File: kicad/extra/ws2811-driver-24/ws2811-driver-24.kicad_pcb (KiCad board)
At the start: 2 copper layers, 140 x 25 mm, 23 parts, among them J1 Conn_01x13_Pin, J2 Conn_01x13_Pin, J3 RJ45 IN, J4 RJ45 OUT, J5 Conn_01x03_Pin, U1 WS2811, U2 WS2811, U3 WS2811, U4 WS2811, U5 WS2811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

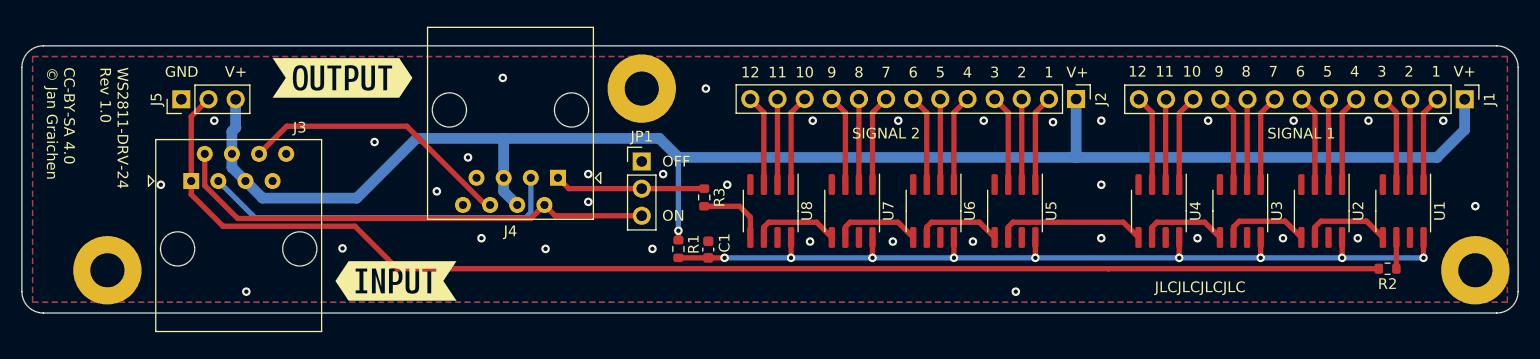
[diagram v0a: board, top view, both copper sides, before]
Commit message: feat: Rework WS2811 boards (Rev 2.0)
* Change RJ45 pinout: The data signal is always paired with a ground
  line to increase signal stability, and the changed wireing eases the
  traces on the boards.

* All WS2811 driver boards have a three pin header for direct drive now.
  They can be directly connected to a signal decoder, e.g. for testing.

* The adapter boards has jumper pins to bypass RJ45 jacks, in case you
  want to connect another board using the final pin header.

* Change pin header component to a better available JCSC parts number.

* Move RJ45 jacks on driver boards a bit more off the board, so that
  there is less space between the jack and the outer side of the Watti
  carrier. This makes it easier to plug in and out RJ45 cables as
  the latches are easier to reach.

Fixes #4
Fixes #5
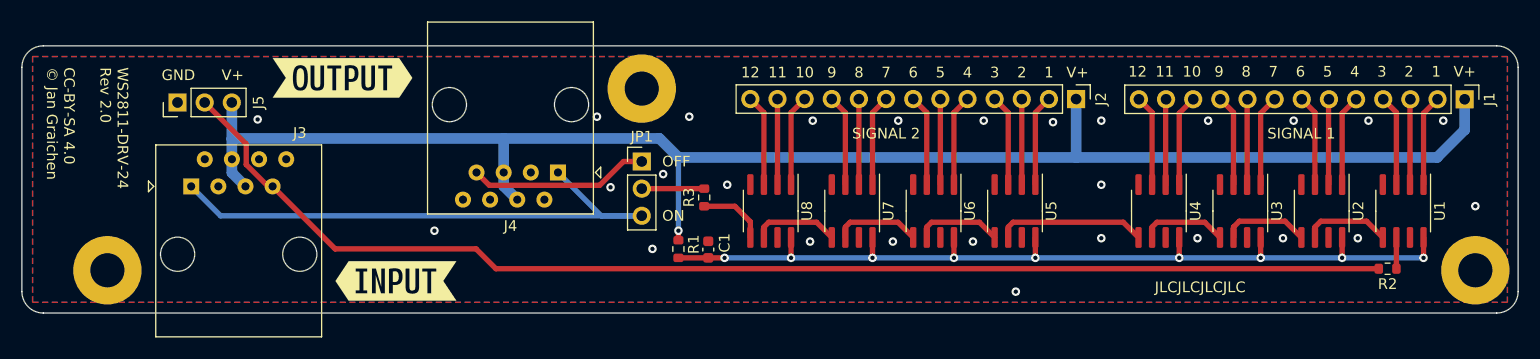
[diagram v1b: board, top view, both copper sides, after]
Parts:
- moved J3 0.50 mm to (92.8, 94.2)
- moved J4 0.50 mm to (127.2, 92.8)
- moved J5 0.47 mm to (91.6, 86.3)
- turned R3 to 90 degrees
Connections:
- J3 pad 1: Net-(J5-Pin_2) -> Net-(JP1-B)
- J3 pad 2: Net-(JP1-B) -> GND
- J3 pad 3: Net-(J3-Pad3) -> GND
- J3 pad 6: Net-(J3-Pad6) -> GND
- J3 pad 7: GND -> Net-(J5-Pin_2)
- J4 pad 1: Net-(JP1-C) -> Net-(JP1-B)
- J4 pad 2: Net-(JP1-B) -> GND
- J4 pad 3: Net-(J3-Pad3) -> GND
- J4 pad 6: Net-(J3-Pad6) -> GND
- J4 pad 7: GND -> Net-(JP1-A)
- JP1 pad 1: unconnected-(JP1-A-Pad1) -> Net-(JP1-A)
- R3 pad 1: Net-(JP1-C) -> Net-(U8-DO)
- R3 pad 2: Net-(U8-DO) -> Net-(JP1-C)
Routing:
- net Net-(J3-Pad3): track 34.1 -> 0.00 mm
- net Net-(J3-Pad6): track 25.7 -> 0.00 mm
- net Net-(JP1-A): track 0.00 -> 16.9 mm
- net Net-(JP1-C): track 14.1 -> 5.84 mm
- net Net-(JP1-B): track 46.1 -> 52.8 mm
- net Net-(J5-Pin_2): track 123.6 -> 117.4 mm
- net VCC: track 150.0 -> 148.3 mm
- net GND: vias 35 -> 27
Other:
- board text added: "WS2811-DRV-24 Rev ${REVISION}"
- board text removed: "WS2811-DRV-24 Rev 1.0"
